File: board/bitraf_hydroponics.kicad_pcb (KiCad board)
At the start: 2 copper layers, 33 parts, among them P1 12V_PWR, P10 ROT_BTN, P11 BUZZ, P12 LDR, P13 MOS_OUT_2, P14 MOS_OUT_1, P15 MOS_OUT_3, P2 I2C_1, P3 I2C_2, P4 I2C_3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

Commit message: Getting on with placing and tracing
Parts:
- added P17: BREAKOUT_1-15, Pin_Headers:Pin_Header_Straight_1x15, F.Cu at (172.7, 116.8)
- added P18: BREAKOUT_16-30, Pin_Headers:Pin_Header_Straight_1x15, F.Cu at (200.7, 81.3)
- C2, C3: footprint Capacitors_ThroughHole:C_Radial_D5_L6_P2.5 -> Capacitors_ThroughHole:C_Disc_D3_P2.5
- P13, P14, P15: footprint Pin_Headers:Pin_Header_Straight_1x02 -> Terminal_Blocks:TerminalBlock_Pheonix_MKDS1.5-2pol
- U2: footprint Power_Integrations:TO-220 -> TO_SOT_Packages_THT:TO-220_Neutral123_Vertical
- moved P8 103.3 mm to (226.1, 94.0), turned to 90 degrees
- moved P6 103.1 mm to (189.2, 153.7), turned to 180 degrees
- moved U1 79.8 mm to (186.7, 99.1)
- moved P5 79.0 mm to (179.1, 153.7), turned to 180 degrees
- moved P10 76.2 mm to (196.8, 153.7), turned to 180 degrees
- moved P9 75.9 mm to (186.7, 126.4)
- moved R3 62.5 mm to (212.1, 113.0), turned to 270 degrees
- moved P2 57.2 mm to (193.0, 126.4)
- moved R5 55.5 mm to (212.1, 99.1), turned to 270 degrees
- moved P3 53.4 mm to (195.6, 126.4)
- moved P12 50.6 mm to (172.7, 153.7), turned to 180 degrees
- moved P4 49.6 mm to (198.1, 126.4)
- moved R4 48.4 mm to (212.1, 127.0), turned to 270 degrees
- moved P7 47.1 mm to (200.7, 126.4)
- moved R1 47.0 mm to (184.2, 143.5), turned to 270 degrees
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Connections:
- net /BUZZ_PIN renamed /BUZZ
- P5 pad 2: /TEMP_HUM_PIN -> (no net)
- P9 pad 1: /SCL -> GND
- P9 pad 3: +12V -> /SCL
- P9 pad 4: GND -> +5V
- U1 pad 1: +5V -> +3V3
- U1 pad 13: Net-(U1-Pad13) -> (no net)
- U1 pad 14: Net-(U1-Pad14) -> (no net)
- U1 pad 17: Net-(U1-Pad17) -> /SCL
- U1 pad 18: Net-(U1-Pad18) -> /SDA
- U1 pad 19: Net-(U1-Pad19) -> /RF_DATA
- U1 pad 20: Net-(U1-Pad20) -> /MOS_3
- U1 pad 23: Net-(U1-Pad23) -> /MOS_2
- U1 pad 24: Net-(U1-Pad24) -> /MOS_1
- U1 pad 25: Net-(U1-Pad25) -> /ROT_SW
- U1 pad 26: Net-(U1-Pad26) -> /ROT_1
- U1 pad 27: Net-(U1-Pad27) -> /ROT_0
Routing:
- net GND: track 37.7 -> 280.8 mm
- net +5V: track 0.00 -> 117.1 mm
- net +12V: track 48.4 -> 130.8 mm
- net /LDR_PIN: track 0.00 -> 78.9 mm
- net /SCL: track 0.00 -> 72.7 mm
- net /SDA: track 0.00 -> 66.4 mm
- net /BUZZ: track 0.00 -> 57.3 mm
- net /ROT_SW: track 0.00 -> 55.5 mm
- net /ROT_1: track 0.00 -> 49.6 mm
- net +3V3: track 0.00 -> 46.5 mm
- net /ROT_0: track 0.00 -> 43.2 mm
- net /MOS_2: track 0.00 -> 31.9 mm
- net /RF_DATA: track 0.00 -> 30.1 mm
- net /MOS_1: track 12.7 -> 40.2 mm, vias 2 -> 0
- net /MOS_3: track 0.00 -> 26.8 mm
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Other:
- net class Default: clearance 0.508 -> 0.4572
- rule trace_clearance: 0.508 -> 0.4572

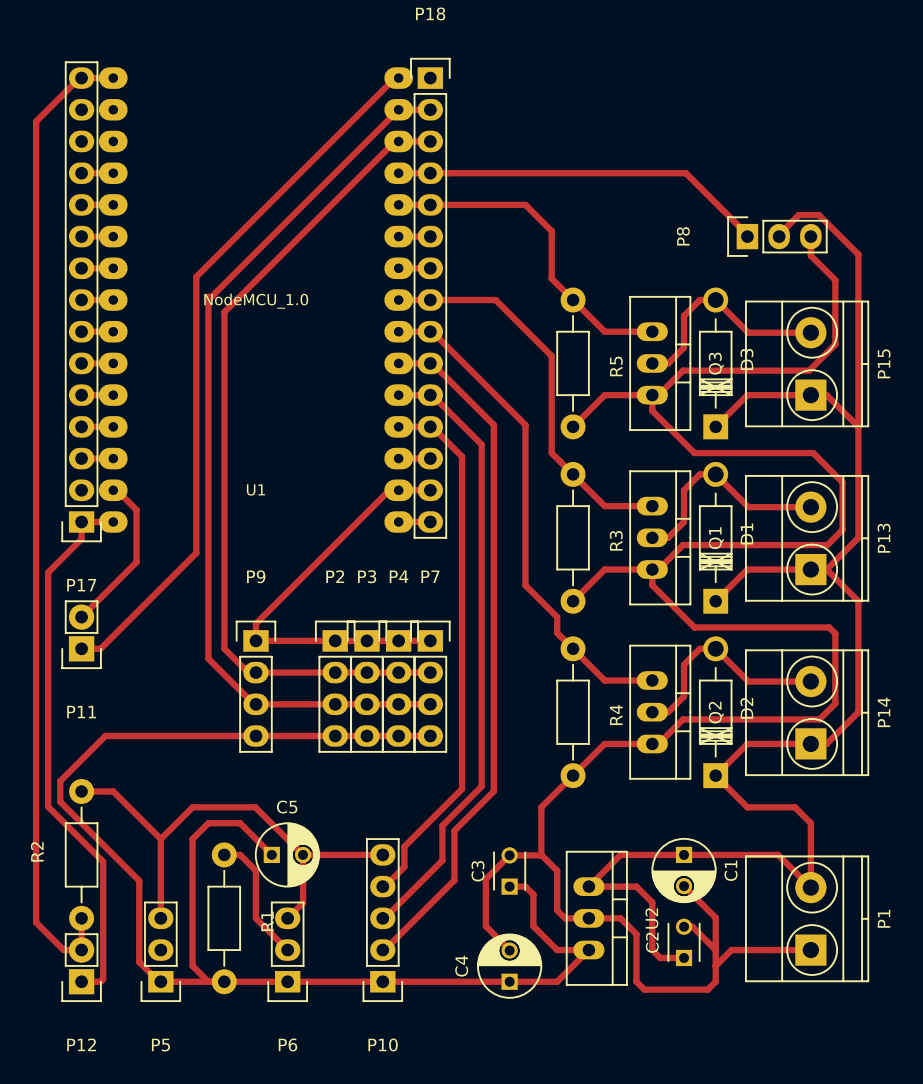
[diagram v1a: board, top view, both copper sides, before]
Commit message: Parts placed and traced. Need to define board and ground plane
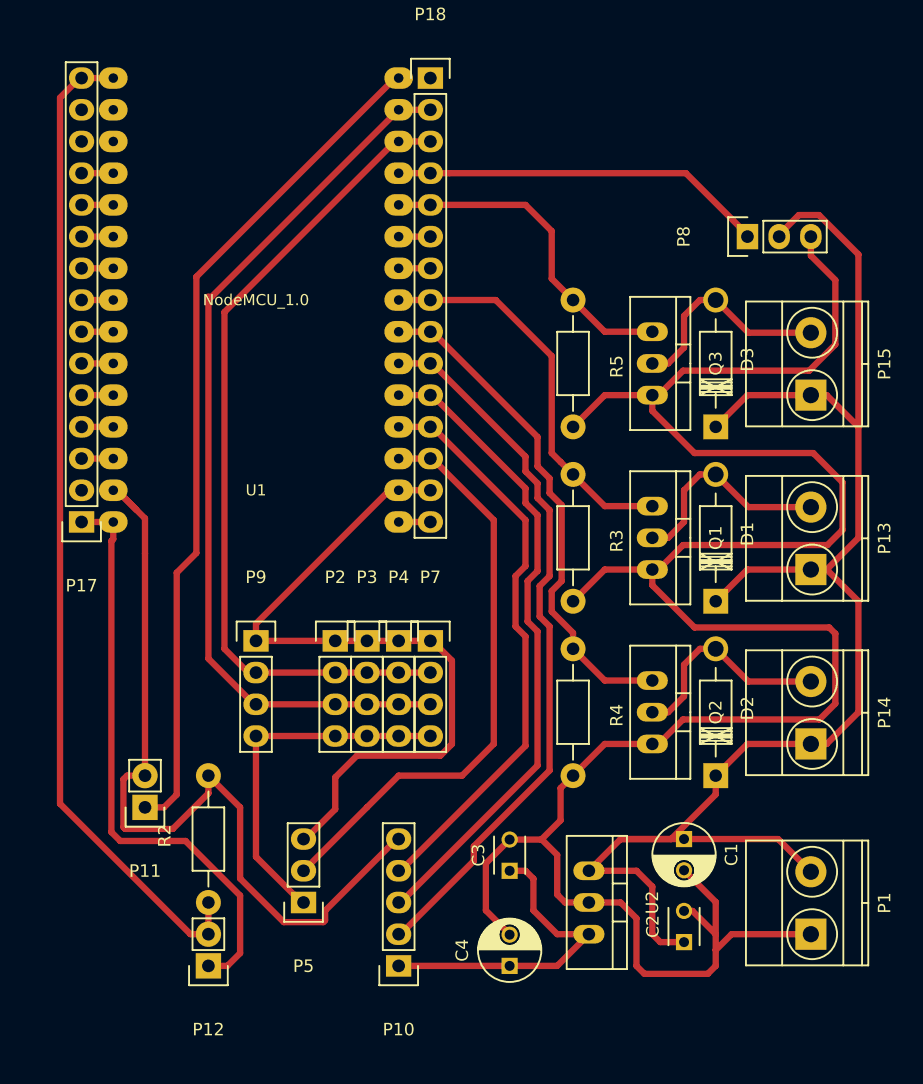
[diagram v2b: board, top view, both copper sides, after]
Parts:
- removed C5: C, Capacitors_ThroughHole:C_Radial_D5_L6_P2.5
- removed P6: TEMP_WTR, Pin_Headers:Pin_Header_Straight_1x03
- removed R1: R, Resistors_ThroughHole:Resistor_Horizontal_RM10mm
- moved P11 13.7 mm to (177.8, 139.7)
- moved P5 13.1 mm to (190.5, 147.3)
- moved R2 10.2 mm to (182.9, 147.3)
- moved P12 10.2 mm to (182.9, 152.4)
- moved P10 1.80 mm to (198.1, 152.4)
- moved C3 1.27 mm to (207.0, 144.8)
- moved U2 1.27 mm to (213.4, 147.3)
- moved C1 1.27 mm to (221.0, 142.2)
- moved C2 1.27 mm to (221.0, 150.5)
- moved C4 1.27 mm to (207.0, 152.4)
- moved P1 1.27 mm to (231.1, 149.9)
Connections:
- P18 pad 13: Net-(P18-Pad13) -> /TEMP_HUM
- P5 pad 2: (no net) -> /TEMP_HUM
- U1 pad 28: Net-(P18-Pad13) -> /TEMP_HUM
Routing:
- net +5V: track 117.1 -> 55.2 mm
- net /TEMP_HUM: track 0.00 -> 47.0 mm
- net GND: track 280.8 -> 319.9 mm
- net /BUZZ: track 57.3 -> 67.9 mm
- net /TEMP_WTR_PIN: track 10.5 -> 0.00 mm
- net +12V: track 130.8 -> 127.0 mm
- net +3V3: track 46.5 -> 50.0 mm
- net /ROT_0: track 43.2 -> 46.3 mm
- net /ROT_SW: track 55.5 -> 58.1 mm
- net /ROT_1: track 49.6 -> 52.2 mm
- net Net-(P18-Pad13): track 2.54 -> 0.00 mm
- net /LDR_PIN: track 78.9 -> 80.2 mm
- net /MOS_1: track 40.2 -> 40.8 mm

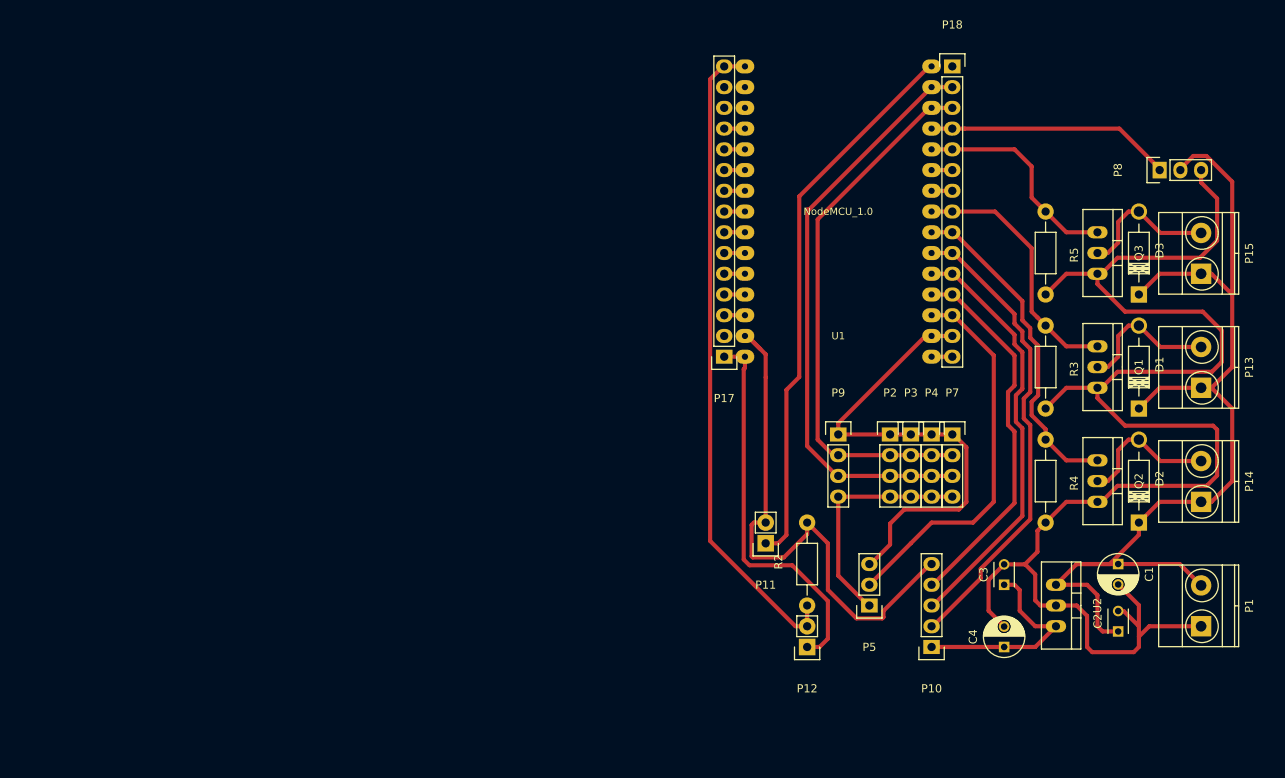
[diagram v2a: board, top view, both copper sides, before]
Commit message: added mounting holes, edge cut and copper fill
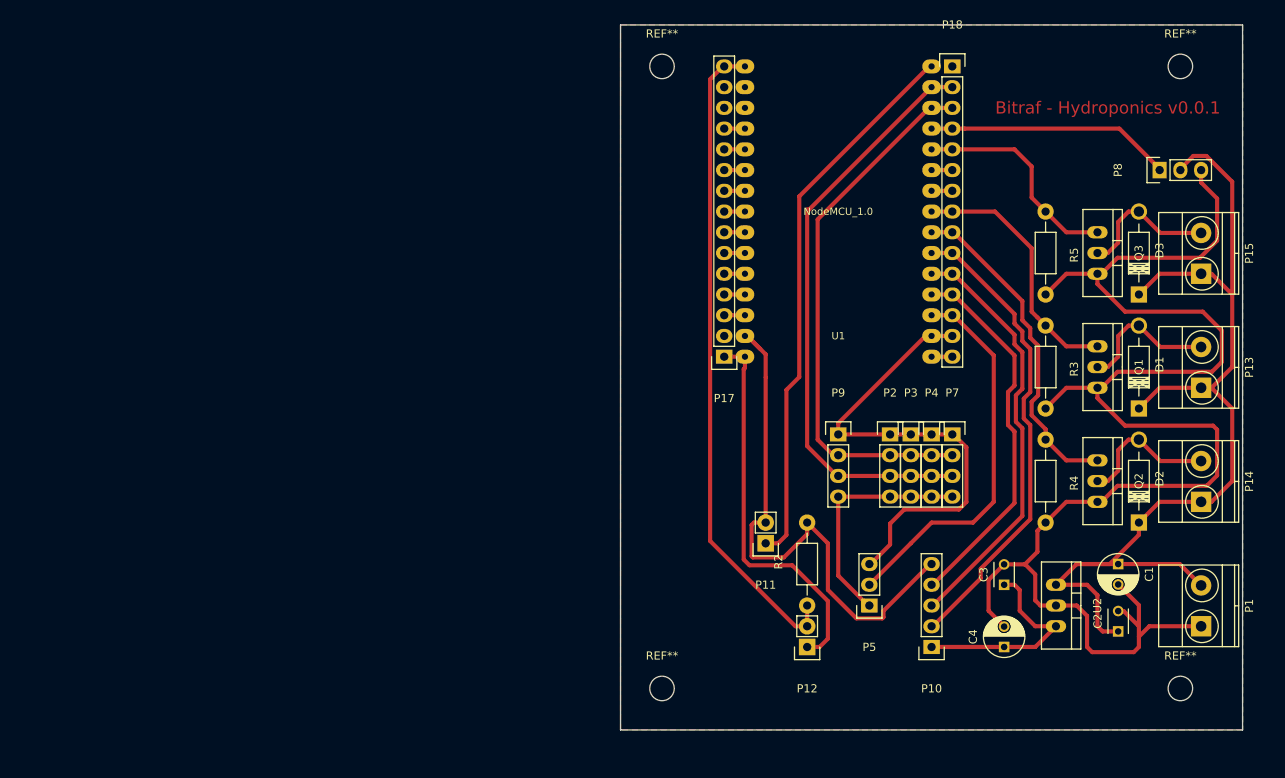
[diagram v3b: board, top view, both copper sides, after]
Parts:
- added REF**: MountingHole_3mm, Mounting_Holes:MountingHole_3mm, F.Cu at (228.6, 81.3)
- added REF**: MountingHole_3mm, Mounting_Holes:MountingHole_3mm, F.Cu at (165.1, 81.3)
- added REF**: MountingHole_3mm, Mounting_Holes:MountingHole_3mm, F.Cu at (165.1, 157.5)
- added REF**: MountingHole_3mm, Mounting_Holes:MountingHole_3mm, F.Cu at (228.6, 157.5)
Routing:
- added copper zone on F.Cu, net (none)
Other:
- board outline added: 76.2 x 86.4 mm
- board text added: "Bitraf - Hydroponics v0.0.1"
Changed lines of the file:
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@@
   (general
     (links 104)
-    (no_connects 26)
-    (area 0 0 0 0)
+    (no_connects 21)
+    (area 159.944999 76.124999 236.295001 162.635001)
     (thickness 1.6)
-    (drawings 0)
+    (drawings 5)
     (tracks 295)
     (zones 0)
-    (modules 32)
+    (modules 36)
     (nets 30)
   )
@@
       (rotate (xyz 0 0 90))
     )
+  )
+  (module Mounting_Holes:MountingHole_3mm (layer F.Cu)
+    (at 228.6 81.28)
+    (descr "Mounting hole, Befestigungsbohrung, 3mm, No Annular, Kein Restring,")
+    (tags "Mounting hole, Befestigungsbohrung, 3mm, No Annular, Kein Restring,")
+    (fp_text reference REF** (at 0 -4.0005) (layer F.SilkS)
+      (effects (font (size 1 1) (thickness 0.15)))
+    )
+    (fp_text value MountingHole_3mm (at -11.43 0) (layer F.Fab)
+      (effects (font (size 1 1) (thickness 0.15)))
+    )
+    (fp_circle (center 0 0) (end 3 0) (layer Cmts.User) (width 0.381))
+    (pad 1 thru_hole circle (at 0 0) (size 3 3) (drill 3) (layers))
+  )
+  (module Mounting_Holes:MountingHole_3mm (layer F.Cu)
+    (at 165.1 81.28)
+    (descr "Mounting hole, Befestigungsbohrung, 3mm, No Annular, Kein Restring,")
+    (tags "Mounting hole, Befestigungsbohrung, 3mm, No Annular, Kein Restring,")
+    (fp_text reference REF** (at 0 -4.0005) (layer F.SilkS)
+      (effects (font (size 1 1) (thickness 0.15)))
+    )
+    (fp_text value MountingHole_3mm (at 10.16 -3.81) (layer F.Fab)
+      (effects (font (size 1 1) (thickness 0.15)))
+    )
+    (fp_circle (center 0 0) (end 3 0) (layer Cmts.User) (width 0.381))
+    (pad 1 thru_hole circle (at 0 0) (size 3 3) (drill 3) (layers))
+  )
+  (module Mounting_Holes:MountingHole_3mm (layer F.Cu)
+    (at 165.1 157.48)
+    (descr "Mounting hole, Befestigungsbohrung, 3mm, No Annular, Kein Restring,")
+    (tags "Mounting hole, Befestigungsbohrung, 3mm, No Annular, Kein Restring,")
+    (fp_text reference REF** (at 0 -4.0005) (layer F.SilkS)
+      (effects (font (size 1 1) (thickness 0.15)))
+    )
+    (fp_text value MountingHole_3mm (at 10.16 2.54) (layer F.Fab)
+      (effects (font (size 1 1) (thickness 0.15)))
+    )
+    (fp_circle (center 0 0) (end 3 0) (layer Cmts.User) (width 0.381))
+    (pad 1 thru_hole circle (at 0 0) (size 3 3) (drill 3) (layers))
+  )
+  (module Mounting_Holes:MountingHole_3mm (layer F.Cu)
+    (at 228.6 157.48)
+    (descr "Mounting hole, Befestigungsbohrung, 3mm, No Annular, Kein Restring,")
+    (tags "Mounting hole, Befestigungsbohrung, 3mm, No Annular, Kein Restring,")
+    (fp_text reference REF** (at 0 -4.0005) (layer F.SilkS)
+      (effects (font (size 1 1) (thickness 0.15)))
+    )
+    (fp_text value MountingHole_3mm (at -10.16 2.54) (layer F.Fab)
+      (effects (font (size 1 1) (thickness 0.15)))
+    )
+    (fp_circle (center 0 0) (end 3 0) (layer Cmts.User) (width 0.381))
+    (pad 1 thru_hole circle (at 0 0) (size 3 3) (drill 3) (layers))
+  )
+  (gr_line (start 160.02 162.56) (end 160.02 76.2) (angle 90) (layer Edge.Cuts) (width 0.15))
+  (gr_line (start 236.22 162.56) (end 160.02 162.56) (angle 90) (layer Edge.Cuts) (width 0.15))
+  (gr_line (start 236.22 76.2) (end 236.22 162.56) (angle 90) (layer Edge.Cuts) (width 0.15))
+  (gr_line (start 160.02 76.2) (end 236.22 76.2) (angle 90) (layer Edge.Cuts) (width 0.15))
+  (gr_text "Bitraf - Hydroponics v0.0.1" (at 219.71 86.36) (layer F.Cu)
+    (effects (font (size 1.5 1.5) (thickness 0.3)))
   )
   (segment (start 223.51746 137.16) (end 223.51746 138.66749) (width 0.508) (layer F.Cu) (net 1))
@@
   (segment (start 195.58 139.7) (end 190.5 144.78) (width 0.508) (layer F.Cu) (net 29))
   (segment (start 198.12 111.76) (end 200.66 111.76) (width 0.508) (layer F.Cu) (net 29))
+  (zone (net 0) (net_name "") (layer F.Cu) (hatch edge 0.508)
+    (connect_pads (clearance 0.508))
+    (min_thickness 0.254)
+    (fill (arc_segments 16) (thermal_gap 0.508) (thermal_bridge_width 0.508))
+    (polygon
+      (pts
+        (xy 160.02 76.2) (xy 236.22 76.2) (xy 236.22 162.56) (xy 160.02 162.56)
+      )
+    )
+  )
 )

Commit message: wip
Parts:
- moved REF** 17.8 mm to (182.9, 81.3)
- moved REF** 10.2 mm to (175.3, 157.5)
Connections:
- P17 pad 13: (no net) -> Net-(P17-Pad13)
- P17 pad 14: (no net) -> Net-(P17-Pad14)
- U1 pad 13: (no net) -> Net-(U1-Pad13)
- U1 pad 14: (no net) -> Net-(U1-Pad14)
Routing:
- net GND: track 319.9 -> 443.5 mm
- net +3V3: track 50.0 -> 72.7 mm
- net +5V: track 55.2 -> 65.9 mm
- net /ROT_0: track 46.3 -> 43.2 mm
- net /ROT_SW: track 58.1 -> 55.0 mm
- net /ROT_1: track 52.2 -> 49.5 mm
- net /BUZZ: track 67.9 -> 70.4 mm
- net /MOS_3: track 26.8 -> 24.5 mm
- net /MOS_2: track 31.9 -> 29.7 mm
- net /TEMP_HUM: track 47.0 -> 45.6 mm
- net /MOS_1: track 40.8 -> 40.2 mm
- net /LDR_PIN: track 80.2 -> 79.7 mm
- added copper zone on B.Cu, net GND
- removed copper zone on F.Cu, net (none)
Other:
- board size 76.2 x 86.4 mm -> 67.3 x 86.4 mm
- net class Default: clearance 0.4572 -> 0.254
- rule trace_clearance: 0.4572 -> 0.254
- rule trace_min: 0.2 -> 0.1
